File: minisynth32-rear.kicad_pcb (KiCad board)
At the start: 2 copper layers, 31.8 x 97.8 mm, 15 parts, among them J1 F_PANEL, J2 Conn_02x20_Odd_Even, J3 PJ-002A, J4 ROT_HDR, J5 MIDI_IN, SW2 PB400EEQR1BLK, U1 H11L1

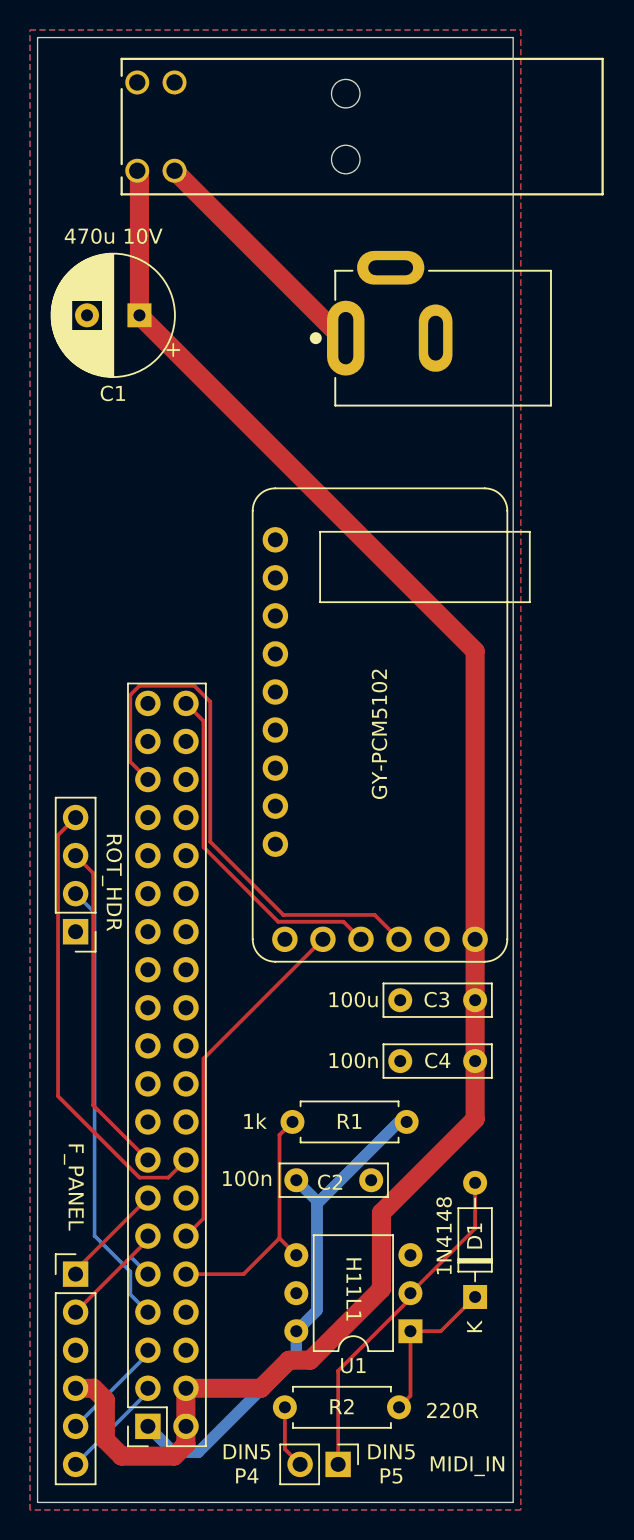
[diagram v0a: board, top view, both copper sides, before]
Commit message: PCB rev 1.1 (rear only): cutaway to support RPi3B
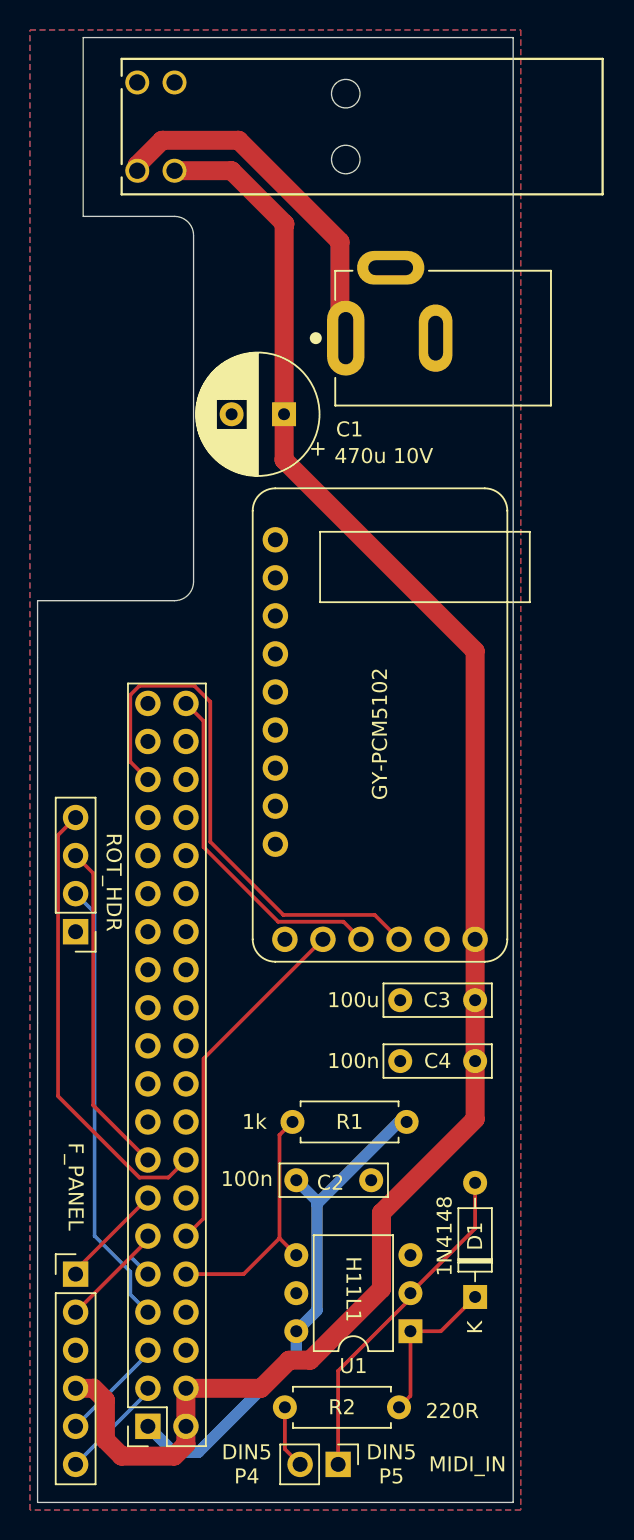
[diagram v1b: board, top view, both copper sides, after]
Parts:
- moved C1 11.7 mm to (146.0, 69.1)
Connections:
- SW2 pad 1: +5V -> Net-(J3-Pad1)
- SW2 pad 2: Net-(J3-Pad1) -> +5V
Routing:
- net Net-(J3-Pad1): track 16.1 -> 24.5 mm
- net +5V: track 117.5 -> 118.7 mm
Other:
- outline, holes or cut-outs redrawn

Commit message: Rev 1.1 F/R PCBs, tuned base and top
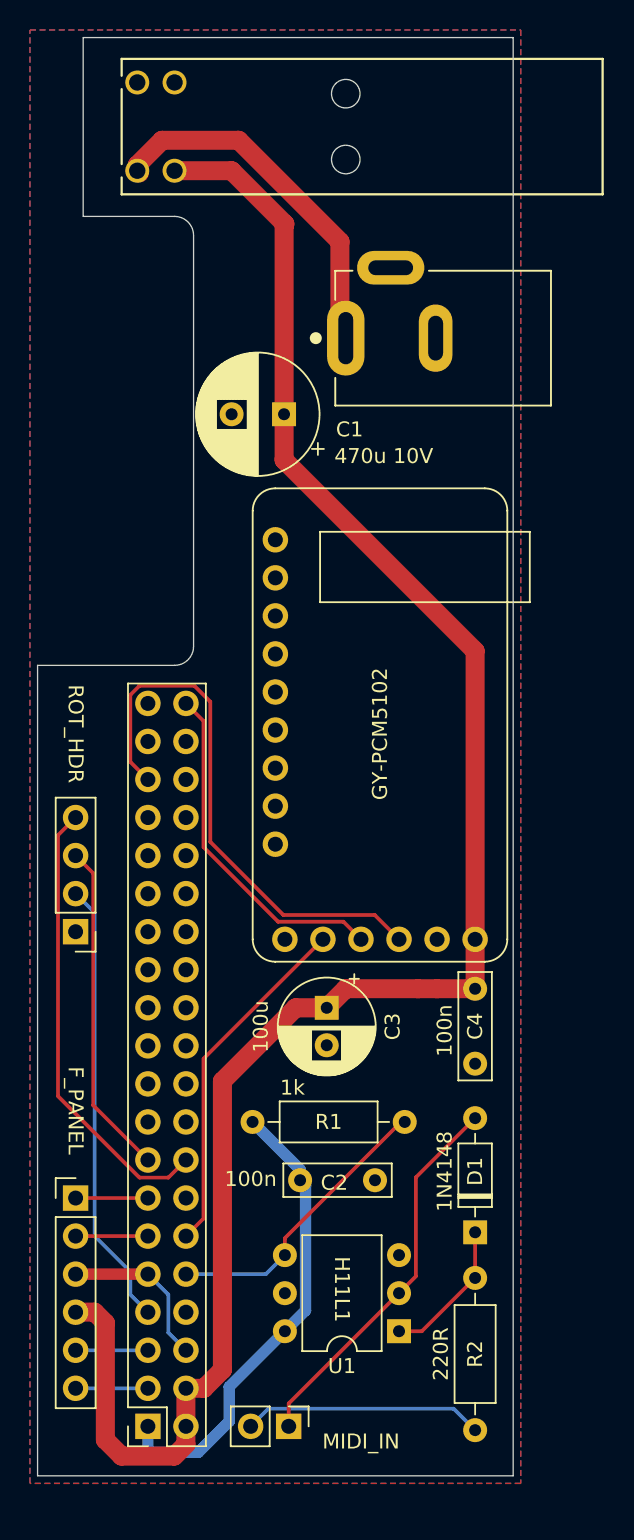
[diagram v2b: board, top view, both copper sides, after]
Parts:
- C3: footprint Capacitor_THT:C_Rect_L7.0mm_W2.0mm_P5.00mm -> Capacitor_THT:CP_Radial_D6.3mm_P2.50mm
- R1, R2: footprint Resistor_THT:R_Axial_DIN0207_L6.3mm_D2.5mm_P7.62mm_Horizontal -> Resistor_THT:R_Axial_DIN0207_L6.3mm_D2.5mm_P10.16mm_Horizontal
- moved R2 12.8 mm to (158.8, 136.9), turned to 90 degrees
- moved C3 9.92 mm to (148.8, 108.7), turned to 270 degrees
- moved R1 7.49 mm to (154.1, 116.3), turned to 180 degrees
- moved J1 5.08 mm to (132.1, 121.4)
- moved C4 4.83 mm to (158.8, 107.4), turned to 270 degrees
- moved D1 4.32 mm to (158.8, 123.7)
- moved J5 4.17 mm to (146.3, 136.7)
- moved U1 0.76 mm to (153.7, 130.3)
- moved C2 0.25 mm to (147.1, 120.2)
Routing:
- net Net-(J5-Pad2): track 4.23 -> 16.1 mm
- net GND: track 1.44 -> 11.0 mm
- net +5V: track 118.7 -> 126.8 mm
- net Net-(D1-Pad2): track 22.6 -> 25.7 mm
- net +3V3: track 34.3 -> 31.5 mm
- net /GPIO15(RXD0): track 16.9 -> 19.5 mm
- net BTN2: track 7.08 -> 4.83 mm
- net BTN1: track 7.08 -> 5.08 mm
- net I2C_SCL: track 7.08 -> 5.08 mm
- net I2C_SDA: track 7.08 -> 5.33 mm
- net Net-(D1-Pad1): track 10.7 -> 9.60 mm
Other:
- board size 31.8 x 97.8 mm -> 31.8 x 96 mm
- board text added: "F_PANEL"
- board text added: "MIDI_IN"
- board text added: "Minisynth 32: Rear panel breakout board https://github.com/grantek/minisynth32 Rev 1.1"
- board text added: "P4"
- board text added: "ROT_HDR"
- board text added: "SDA SCL VCC GND B1 B2"
- board text removed: "DIN5 P4"
- board text removed: "Minisynth 32: Rear panel breakout board https://github.com/grantek/minisynth32"
- board text removed: "SDA SCL"
- board text removed: "VCC GND B1 B2"
